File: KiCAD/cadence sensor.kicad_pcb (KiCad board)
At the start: 2 copper layers, 20 x 64.5 mm, 41 parts, among them J1 USB_C_Receptacle_USB2.0_16P, J2 JST_BATT, J4 JST_SOL, SW1 SW_Push, SW2 SW_PWR, U1 ESP32-S3-WROOM-1-N4, U2 TPD4E05U06DQA, U7 BQ25570

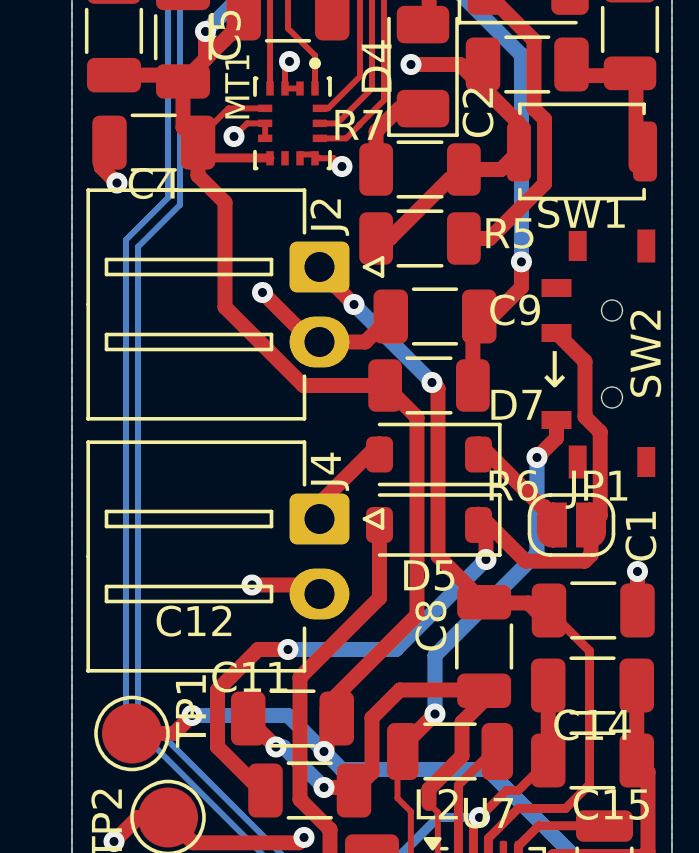
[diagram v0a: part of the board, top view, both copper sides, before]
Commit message: KiCAD use local modified of footprint for JST connector
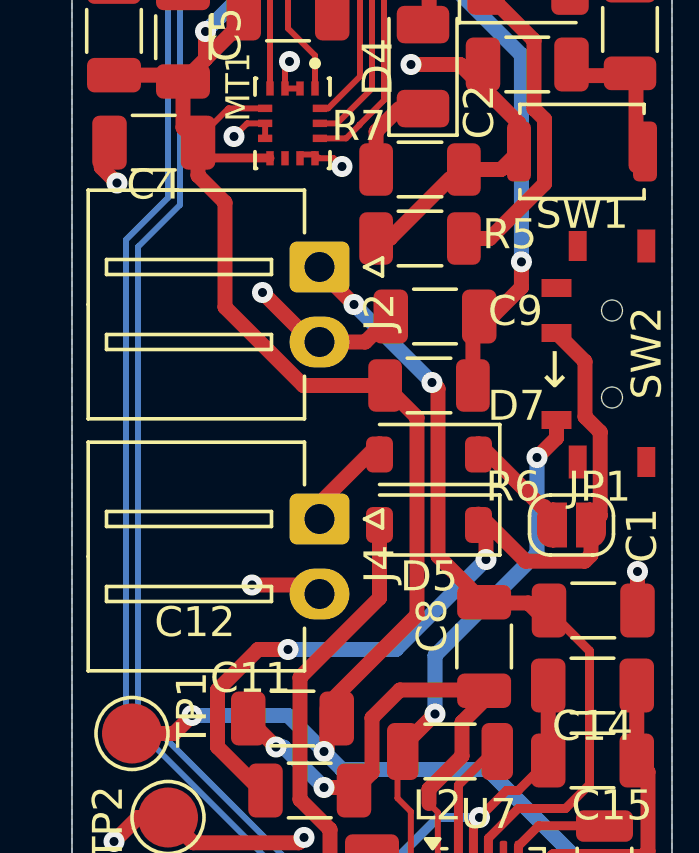
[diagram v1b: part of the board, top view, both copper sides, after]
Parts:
- J2, J4: footprint JST2:JST_XH_S2B-XH-A-1_1x02_P2.50mm_Horizontal_2 -> Connector_JST:JST_XH_S2B-XH-A-1_1x02_P2.50mm_Horizontal
